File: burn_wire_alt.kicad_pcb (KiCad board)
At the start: 2 copper layers, 16 parts, among them U1 ADP2303ARDZ

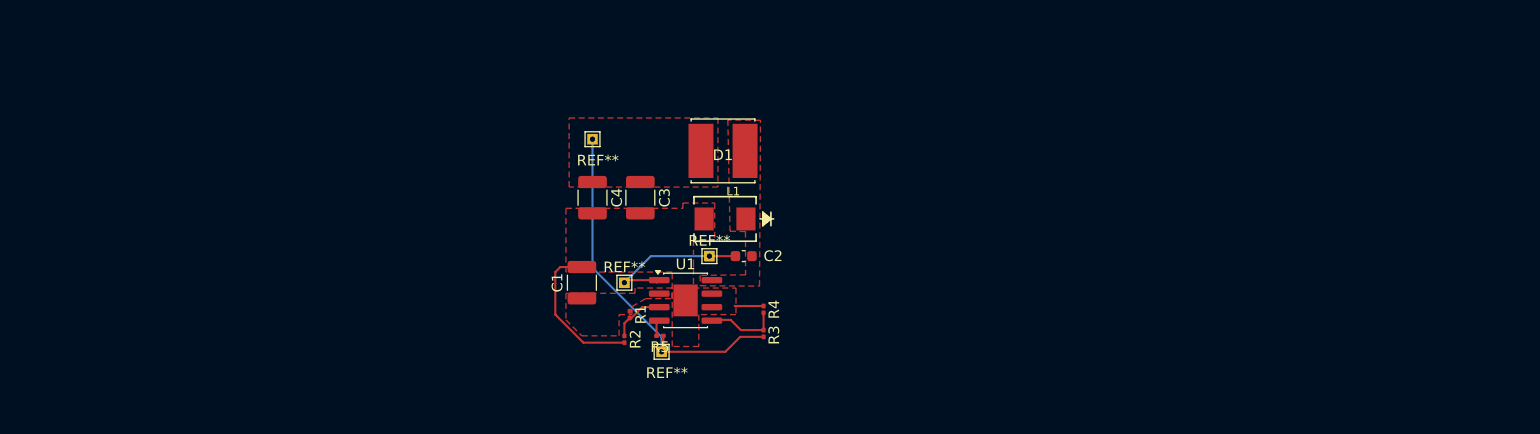
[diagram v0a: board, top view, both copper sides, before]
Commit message: polished layout, agrees with datasheet layout, mostly agrees with buck layout recs article
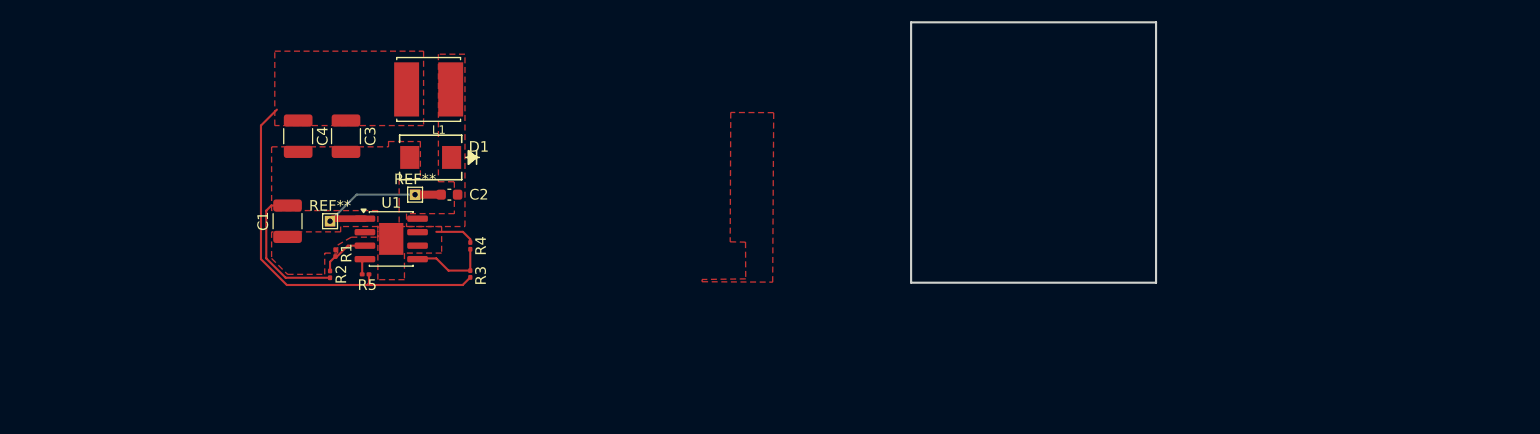
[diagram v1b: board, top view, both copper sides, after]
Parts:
- removed the REF** at (200.5, 96.0)
- removed the REF** at (192.5, 98.5)
- removed the REF** at (196.0, 105.0)
- removed the REF** at (189.5, 85.0)
- added REF**: TestPoint_THTPad_1.0x1.0mm_Drill0.5mm, TestPoint:TestPoint_THTPad_1.0x1.0mm_Drill0.5mm, F.Cu at (172.8, 90.2)
- added REF**: TestPoint_THTPad_1.0x1.0mm_Drill0.5mm, TestPoint:TestPoint_THTPad_1.0x1.0mm_Drill0.5mm, F.Cu at (164.8, 92.7)
- moved R2 28.4 mm to (164.8, 97.7)
- moved C1 28.3 mm to (160.8, 92.7)
- moved C3 28.3 mm to (166.3, 84.7)
- moved C4 28.3 mm to (161.8, 84.7)
- moved D1 28.3 mm to (174.3, 86.7)
- moved L1 28.3 mm to (174.1, 80.3)
- moved R1 28.3 mm to (165.3, 95.7)
- moved R5 28.3 mm to (168.2, 97.7)
- moved U1 28.3 mm to (170.6, 94.4)
- moved C2 28.3 mm to (176.0, 90.2)
- moved R4 28.2 mm to (178.0, 95.0)
- moved R3 28.2 mm to (178.0, 97.7)
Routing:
- net /Vout: track 34.4 -> 37.0 mm
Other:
- board outline added: 23 x 24.5 mm

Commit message: forgot to save changes before pushing
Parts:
- moved C2 4.41 mm to (174.7, 86.0)
- moved J2 4.41 mm to (171.5, 86.0)
- moved C1 4.20 mm to (165.0, 92.5)
- moved J1 4.12 mm to (168.1, 90.2)
- moved D1 2.80 mm to (174.0, 89.5)
- moved C4 2.31 mm to (164.0, 84.0)
- moved C3 1.84 mm to (168.0, 84.0)
- renumbered REF** to J1, REF** to J2
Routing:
- net /BST: track 14.9 -> 10.3 mm
- net /Vout: track 37.0 -> 39.2 mm
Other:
- board text added: "Question/notes/remarks: - no clue if test point jumper wires are big enough for the power we need ( i think it should be fine) - maybe we want to also route the feedback to the back as well (minimize switching noise) - according to the internet (pcb layout for bucks article), the gnds of Cout and Cin should is recommended to be 1-2 cm apart bc noise propagation"
- board text added: "power gnd"
- board text added: "signal gnd"
